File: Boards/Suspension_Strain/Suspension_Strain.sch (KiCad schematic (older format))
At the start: 37 parts, among them J1 CONN_02X03, J101 MM_F_RA_20, J102 MM_F_RA_08, U1 MCP2561-E_SN, U101 TPS560430YF, U102 74HC4051, U2 ATMEGA16M1, Y1 Crystal_SMD

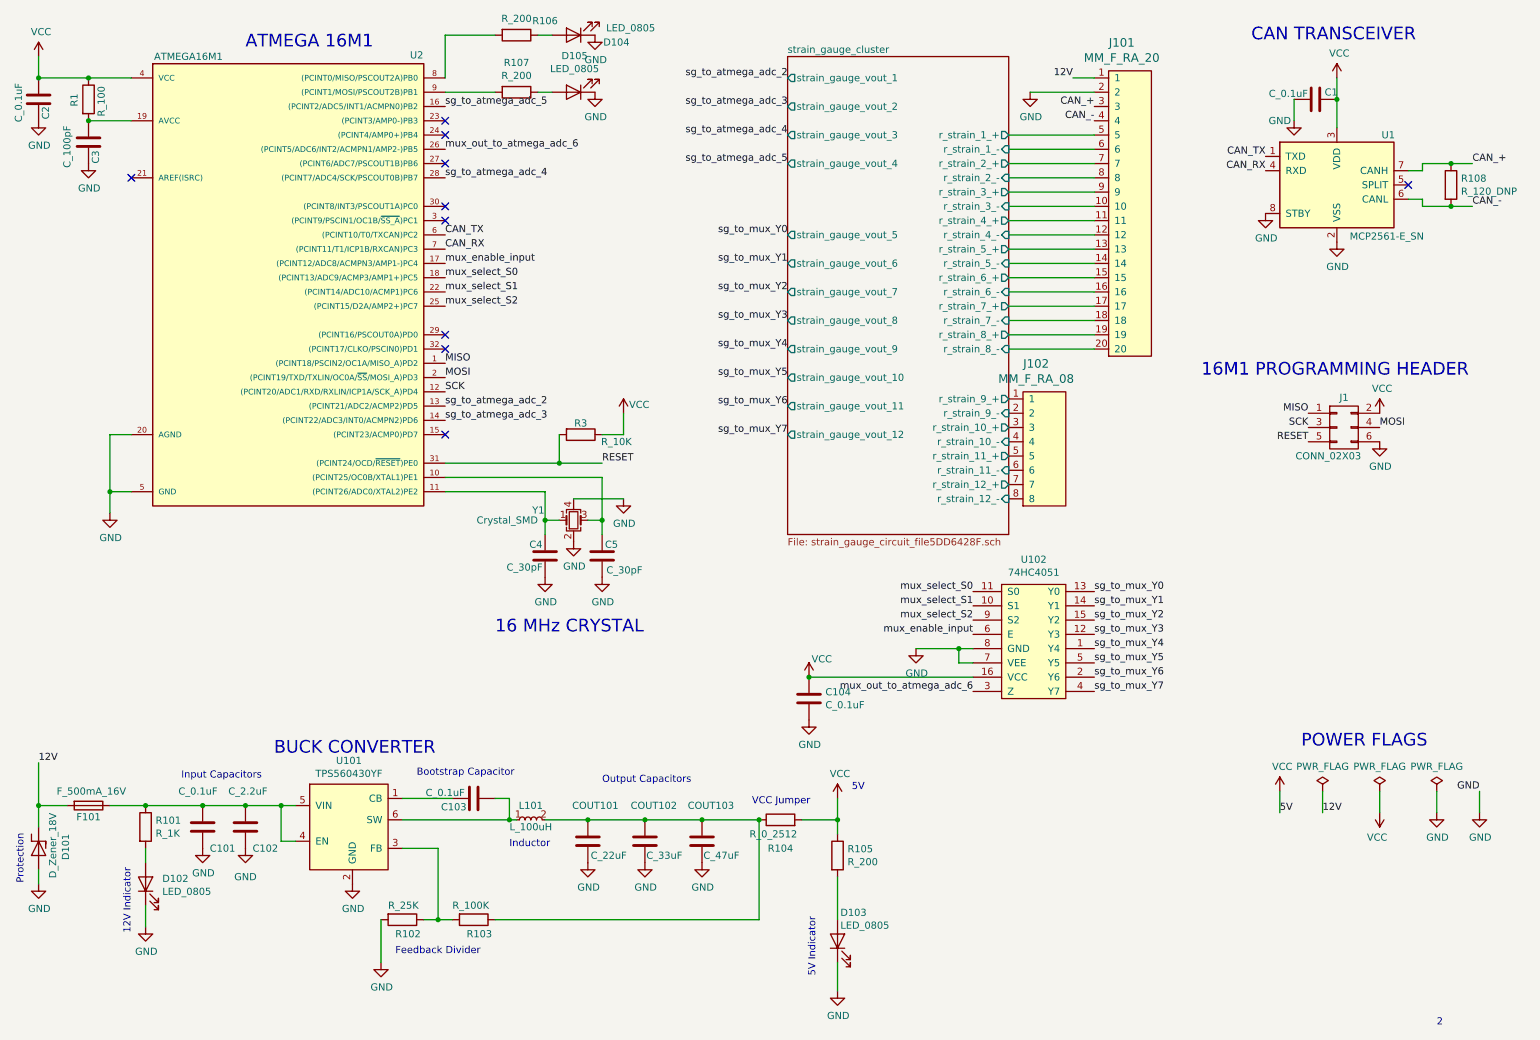
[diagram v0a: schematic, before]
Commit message: Remove excessive differential amplifiers
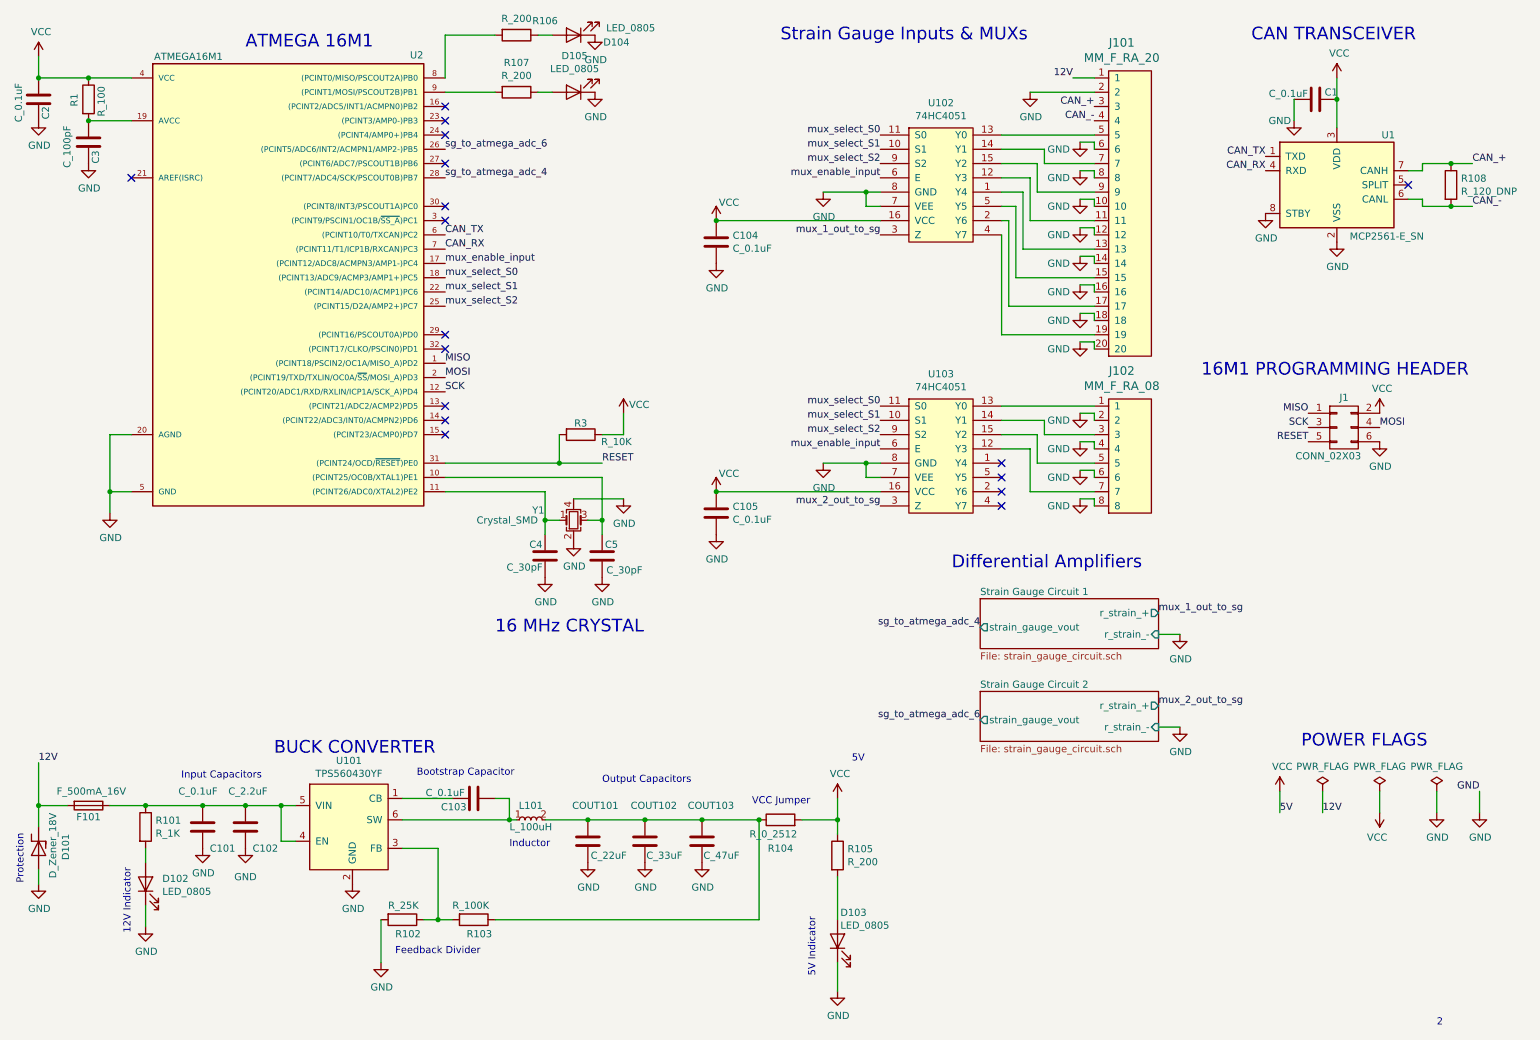
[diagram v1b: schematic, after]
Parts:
- added C105: C_0.1uF, footprints:C_0805_OEM, symbol Formula:C_0.1uF
- added U103: 74HC4051, footprints:TSSOP-16-OEM, symbol Formula:74HC4051
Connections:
- net strain_gauge_cluster/r_strain_10_- is gone; now on net GND: J102.4
- net strain_gauge_cluster/r_strain_11_- is gone; now on net GND: J102.6
- net strain_gauge_cluster/r_strain_12_- is gone; now on net GND: J102.8
- net strain_gauge_cluster/r_strain_1_+ is gone; now on an unnamed net: J101.5
- net strain_gauge_cluster/r_strain_1_- is gone; now on net GND: J101.6
- net strain_gauge_cluster/r_strain_2_+ is gone; now on an unnamed net: J101.7
- net strain_gauge_cluster/r_strain_2_- is gone; now on net GND: J101.8
- net strain_gauge_cluster/r_strain_3_+ is gone; now on an unnamed net: J101.9
- net strain_gauge_cluster/r_strain_3_- is gone; now on net GND: J101.10
- net strain_gauge_cluster/r_strain_4_+ is gone; now on an unnamed net: J101.11
- net strain_gauge_cluster/r_strain_4_- is gone; now on net GND: J101.12
- net strain_gauge_cluster/r_strain_5_+ is gone; now on an unnamed net: J101.13
- net strain_gauge_cluster/r_strain_5_- is gone; now on net GND: J101.14
- net strain_gauge_cluster/r_strain_6_+ is gone; now on an unnamed net: J101.15
- net strain_gauge_cluster/r_strain_6_- is gone; now on net GND: J101.16
- net strain_gauge_cluster/r_strain_7_+ is gone; now on an unnamed net: J101.17
- net strain_gauge_cluster/r_strain_7_- is gone; now on net GND: J101.18
- net strain_gauge_cluster/r_strain_8_+ is gone; now on an unnamed net: J101.19
- net strain_gauge_cluster/r_strain_8_- is gone; now on net GND: J101.20
- net strain_gauge_cluster/r_strain_9_- is gone; now on net GND: J102.2
- net GND: now also C105.2, U103.7 (VEE), U103.8 (GND)
- net VCC: now also C105.1, U103.16 (VCC)
- net mux_enable_input: now also U103.6 (E)
- net mux_select_S0: now also U103.11 (S0)
- net mux_select_S1: now also U103.10 (S1)
- net mux_select_S2: now also U103.9 (S2)
- net mux_out_to_atmega_adc_6 renamed mux_1_out_to_sg
- net mux_1_out_to_sg: no longer U2.26 ((PCINT5/ADC6/INT2/ACMPN1/AMP2-)PB5)
- net sg_to_atmega_adc_2: no longer names the net of U2.13 ((PCINT21/ADC2/ACMP2)PD5)
- net sg_to_atmega_adc_3: no longer names the net of U2.14 ((PCINT22/ADC3/INT0/ACMPN2)PD6)
- net sg_to_atmega_adc_5: no longer names the net of U2.16 ((PCINT2/ADC5/INT1/ACMPN0)PB2)
- net sg_to_mux_Y0: no longer names the net of U102.13 (Y0)
- net sg_to_mux_Y1: no longer names the net of U102.14 (Y1)
- net sg_to_mux_Y2: no longer names the net of U102.15 (Y2)
- net sg_to_mux_Y3: no longer names the net of U102.12 (Y3)
- net sg_to_mux_Y4: no longer names the net of U102.1 (Y4)
- net sg_to_mux_Y5: no longer names the net of U102.5 (Y5)
- net sg_to_mux_Y6: no longer names the net of U102.2 (Y6)
- net sg_to_mux_Y7: no longer names the net of U102.4 (Y7)
- net strain_gauge_cluster/r_strain_10_+: no longer names the net of J102.3
- net strain_gauge_cluster/r_strain_10_+: now also U103.14 (Y1)
- net strain_gauge_cluster/r_strain_11_+: no longer names the net of J102.5
- net strain_gauge_cluster/r_strain_11_+: now also U103.15 (Y2)
- net strain_gauge_cluster/r_strain_12_+: no longer names the net of J102.7
- net strain_gauge_cluster/r_strain_12_+: now also U103.12 (Y3)
- net strain_gauge_cluster/r_strain_9_+: no longer names the net of J102.1
- net strain_gauge_cluster/r_strain_9_+: now also U103.13 (Y0)
- new net mux_2_out_to_sg: U103.3 (Z)
- new net sg_to_atmega_adc_6: U2.26 ((PCINT5/ADC6/INT2/ACMPN1/AMP2-)PB5)
- no-connect marks 10 -> 17
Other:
- note added: "Differential Amplifiers"
- note added: "Strain Gauge Inputs & MUXs"
- moved on the sheet: C104, J102, U102

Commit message: Add in-progress changes for reducing noise and component use
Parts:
- removed C104, C105: C_0.1uF, footprints:C_0805_OEM, symbol Formula:C_0.1uF
- removed U102, U103: 74HC4051, footprints:TSSOP-16-OEM, symbol Formula:74HC4051
- added R?: R_120, footprints:R_0805_OEM, symbol Formula:R_120
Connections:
- net VCC: now also R?.1
- net wsb_container/s9_+: now reaches J102.1
- net wsb_container/s10_+: now reaches J102.3
- net wsb_container/s11_+: now reaches J102.5
- net wsb_container/s12_+: now reaches J102.7
- net wsb_container/s4_+: now reaches J101.11
- net wsb_container/s5_+: now reaches J101.13
- net wsb_container/s6_+: now reaches J101.15
- net wsb_container/s7_+: now reaches J101.17
- net wsb_container/s8_+: now reaches J101.19
- net wsb_container/s1_+: now reaches J101.5
- net wsb_container/s2_+: now reaches J101.7
- net wsb_container/s3_+: now reaches J101.9
- net sg_to_atmega_adc_4 renamed amp_1_out
- net sg_to_atmega_adc_6 renamed amp_2_out
- new net VCC_ANALOG: R?.2
- no-connect marks 17 -> 13
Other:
- note added: "<- make ferrite"
- note added: "Inputs"
- note added: "Outputs"
- note removed: "Differential Amplifiers"
- moved on the sheet: C4, C5, J1, J101, J102, R3, Y1
